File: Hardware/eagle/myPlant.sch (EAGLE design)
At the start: 38 parts, among them U1 SI7021, U2 ALS-PT19, U3 FSA3357, U4 TPS22860, U5 NCP1402, X1 ESP-12

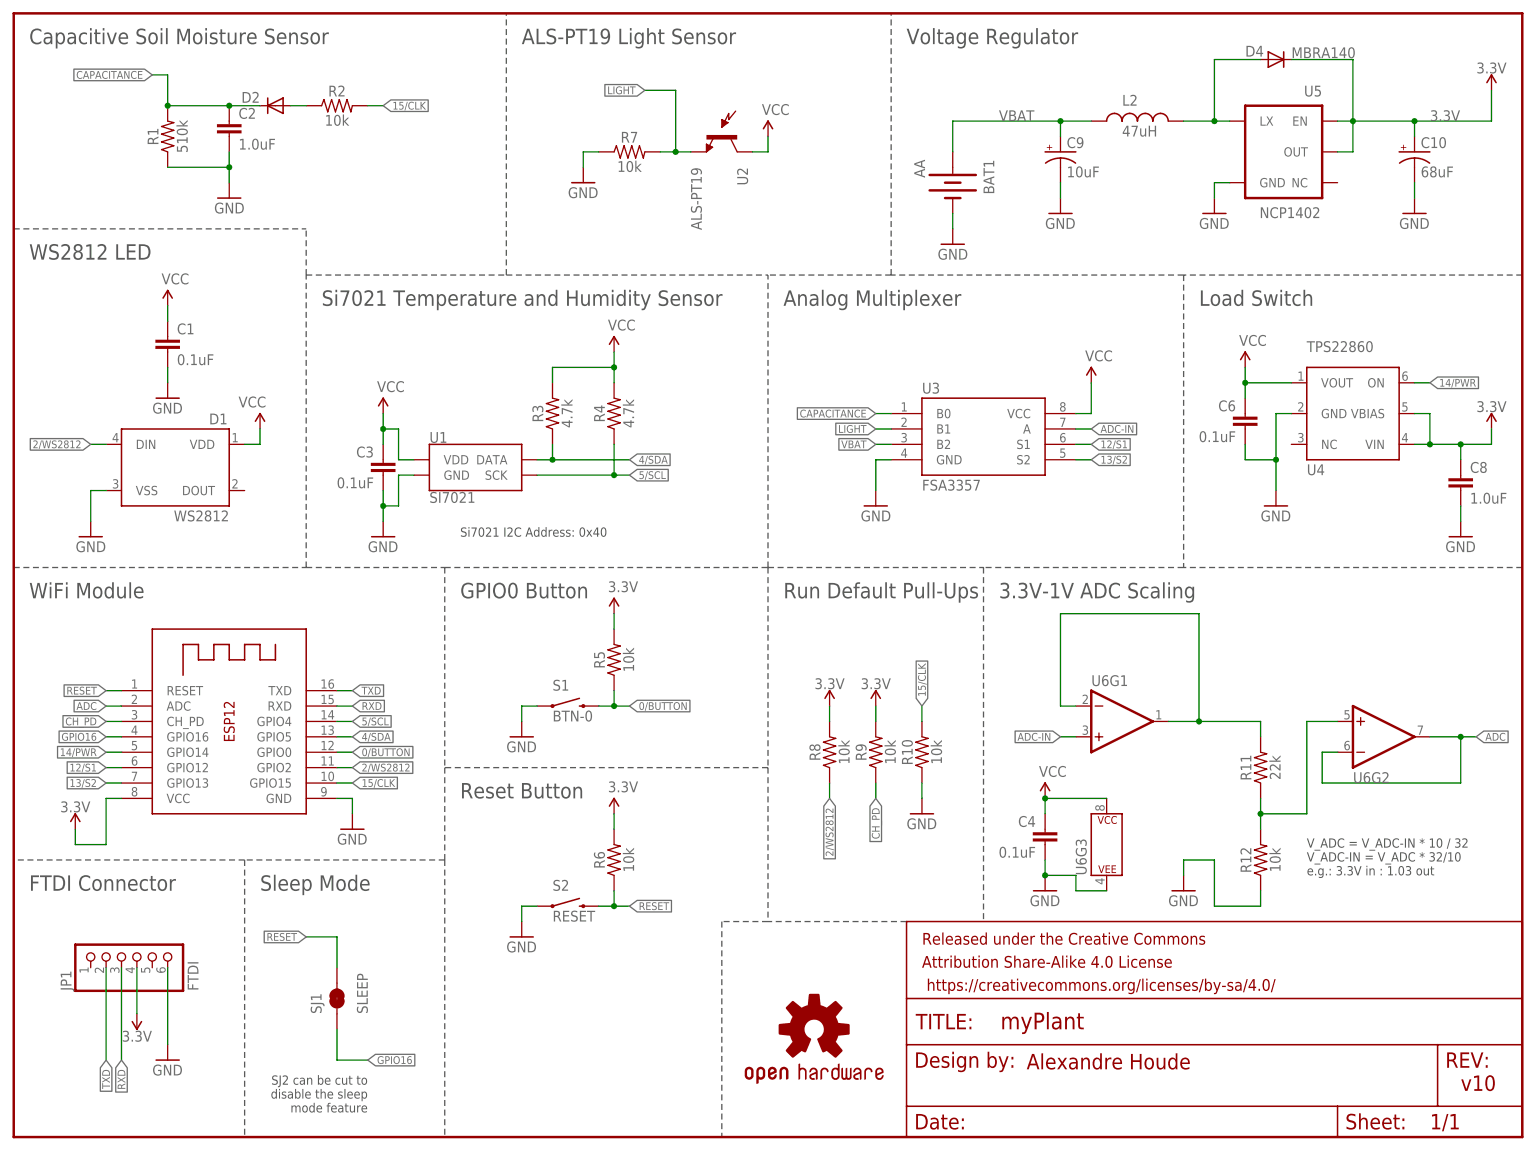
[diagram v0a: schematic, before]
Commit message: Corrected DRC errors
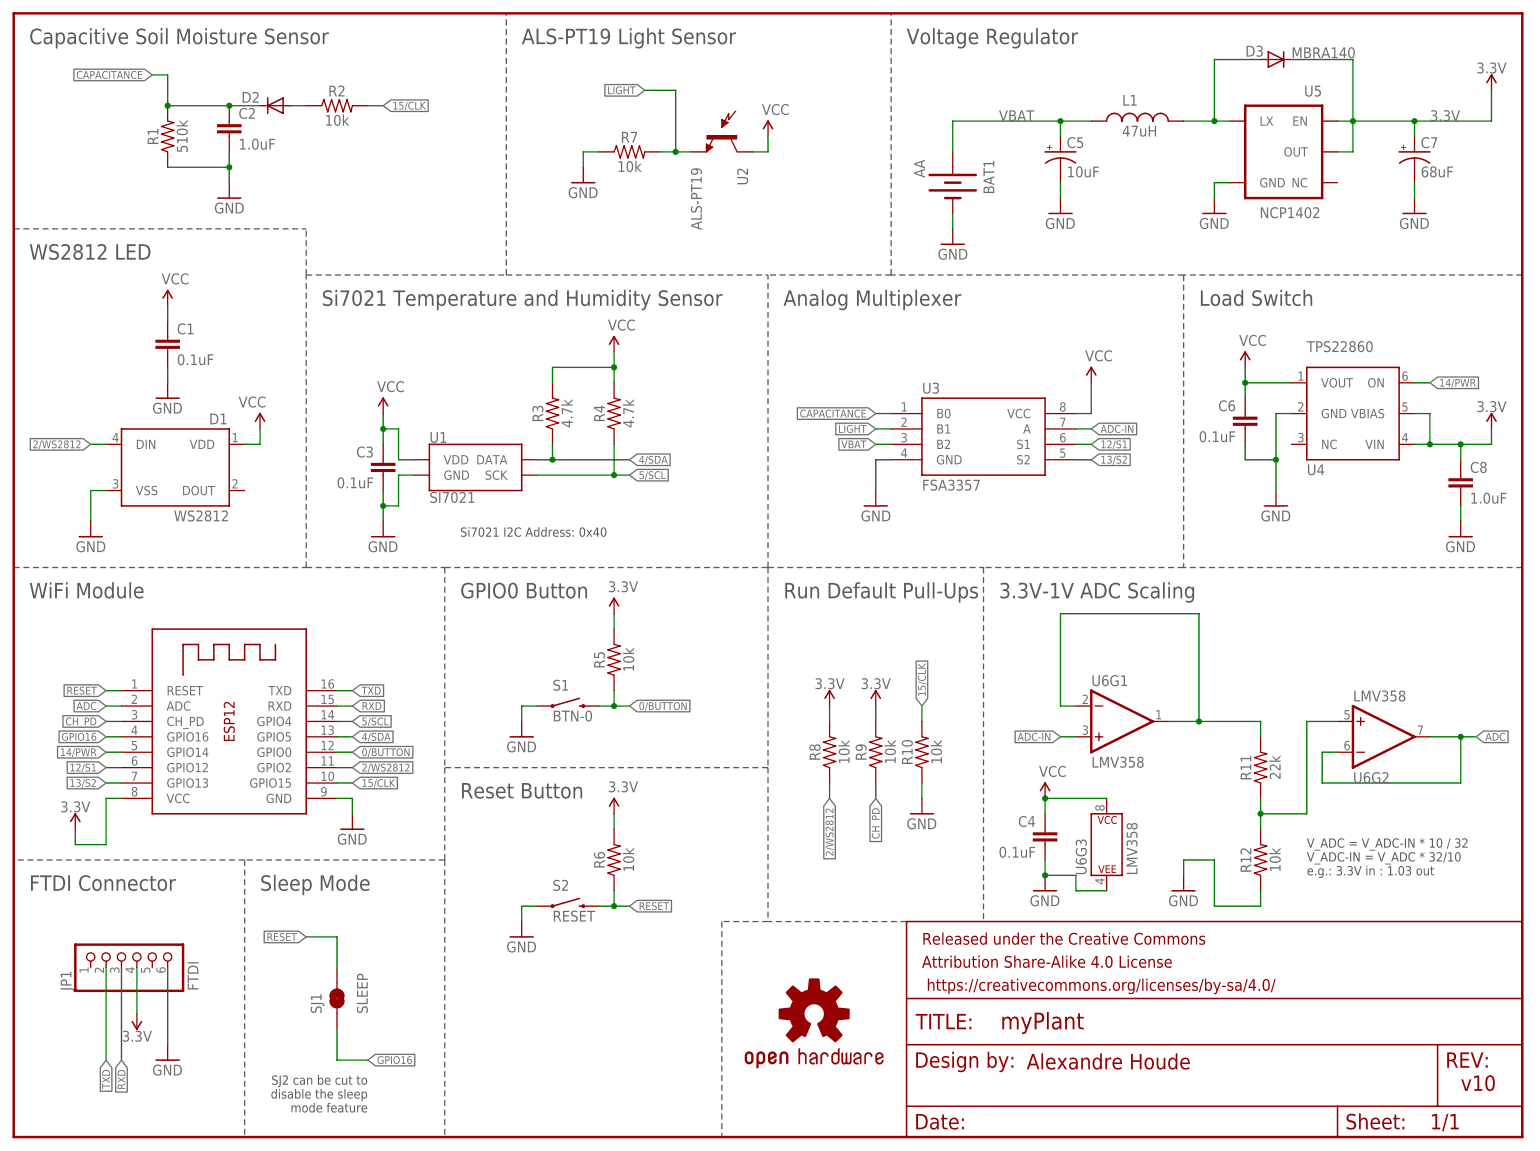
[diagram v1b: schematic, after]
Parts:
- removed LOGO1: OSHW-LOGOM, SparkFun-Aesthetics:OSHW-LOGOM
- added LOGO2: OSHW-LOGOS, SparkFun-Aesthetics:OSHW-LOGOS
- U6: value (none) -> LMV358
- renumbered C10 to C7, C9 to C5, D4 to D3, L2 to L1
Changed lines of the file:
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@@
 <?xml version="1.0" encoding="utf-8"?>
 <!DOCTYPE eagle SYSTEM "eagle.dtd">
-<eagle version="8.2.1">
+<eagle version="8.2.2">
 <drawing>
 <settings>
@@
 </layers>
 <schematic xreflabel="%F%N/%S.%C%R" xrefpart="/%S.%C%R">
-<description>Plant watering alarm v2.4</description>
 <attributes>
 </attributes>
@@
 <part name="GND20" library="SparkFun-Aesthetics" deviceset="GND" device=""/>
 <part name="FRAME1" library="SparkFun-Aesthetics" deviceset="FRAME-LETTER" device=""/>
-<part name="LOGO1" library="SparkFun-Aesthetics" deviceset="OSHW-LOGO" device="M"/>
 <part name="SUPPLY16" library="SparkFun-PowerSymbols" deviceset="3.3V" device=""/>
 <part name="SUPPLY17" library="SparkFun-PowerSymbols" deviceset="3.3V" device=""/>
@@
 <part name="C4" library="SparkFun-Capacitors" deviceset="0.1UF" device="-0603-25V-(+80/-20%)" value="0.1uF"/>
 <part name="U5" library="SparkFun" deviceset="V_REG_NCP1400" device="SOT23-5" value="NCP1402"/>
-<part name="D4" library="SparkFun" deviceset="DIODE" device="SMA" value="MBRA140"/>
-<part name="C9" library="SparkFun" deviceset="CAP_POL" device="1206" value="10uF"/>
-<part name="C10" library="SparkFun" deviceset="CAP_POL" device="3528" value="68uF"/>
-<part name="L2" library="SparkFun" deviceset="INDUCTOR" device="CR54" value="47uH"/>
+<part name="D3" library="SparkFun" deviceset="DIODE" device="SMA" value="MBRA140"/>
+<part name="C5" library="SparkFun" deviceset="CAP_POL" device="1206" value="10uF"/>
+<part name="C7" library="SparkFun" deviceset="CAP_POL" device="3528" value="68uF"/>
+<part name="L1" library="SparkFun" deviceset="INDUCTOR" device="CR54" value="47uH"/>
 <part name="GND22" library="SparkFun" deviceset="GND" device=""/>
 <part name="GND23" library="SparkFun" deviceset="GND" device=""/>
 <part name="GND24" library="SparkFun" deviceset="GND" device=""/>
-<part name="U6" library="SparkFun-IC-Amplifiers" deviceset="LMV358" device=""/>
+<part name="U6" library="SparkFun-IC-Amplifiers" deviceset="LMV358" device="" value="LMV358"/>
+<part name="LOGO2" library="SparkFun-Aesthetics" deviceset="OSHW-LOGO" device="S" value="OSHW-LOGOS"/>
 </parts>
 <sheets>
 <sheet>
-<description>Plant watering alarm v1.0</description>
 <plain>
 <text x="73.66" y="99.06" size="1.524" layer="97">Si7021 I2C Address: 0x40</text>
@@
 <instance part="FRAME1" gate="G$1" x="0" y="0"/>
 <instance part="FRAME1" gate="V" x="147.32" y="0"/>
-<instance part="LOGO1" gate="G$1" x="132.08" y="17.78"/>
 <instance part="SUPPLY16" gate="G$1" x="243.84" y="172.72"/>
 <instance part="SUPPLY17" gate="G$1" x="243.84" y="116.84"/>
@@
 <instance part="C4" gate="G$1" x="170.18" y="48.26" rot="MR0"/>
 <instance part="U5" gate="G$1" x="210.82" y="162.56" rot="MR0"/>
-<instance part="D4" gate="G$1" x="208.28" y="177.8" smashed="yes">
+<instance part="D3" gate="G$1" x="208.28" y="177.8" smashed="yes">
 <attribute name="NAME" x="203.2" y="178.2826" size="1.778" layer="95"/>
 <attribute name="VALUE" x="210.82" y="178.0286" size="1.778" layer="96"/>
 </instance>
-<instance part="C9" gate="G$1" x="172.72" y="162.56"/>
-<instance part="C10" gate="G$1" x="231.14" y="162.56"/>
-<instance part="L2" gate="G$1" x="185.42" y="167.64" smashed="yes" rot="R90">
+<instance part="C5" gate="G$1" x="172.72" y="162.56"/>
+<instance part="C7" gate="G$1" x="231.14" y="162.56"/>
+<instance part="L1" gate="G$1" x="185.42" y="167.64" smashed="yes" rot="R90">
 <attribute name="NAME" x="182.88" y="170.18" size="1.778" layer="95"/>
 <attribute name="VALUE" x="182.88" y="165.1" size="1.778" layer="96"/>
@@
 <instance part="U6" gate="G2" x="226.06" y="66.04" rot="MR180"/>
 <instance part="U6" gate="G3" x="180.34" y="48.26"/>
+<instance part="LOGO2" gate="G$1" x="132.08" y="20.32"/>
 </instances>
 <busses>
@@
 <segment>
 <wire x1="231.14" y1="157.48" x2="231.14" y2="154.94" width="0.1524" layer="91"/>
-<pinref part="C10" gate="G$1" pin="-"/>
+<pinref part="C7" gate="G$1" pin="-"/>
 <pinref part="GND24" gate="1" pin="GND"/>
 </segment>
@@
 <segment>
 <wire x1="172.72" y1="157.48" x2="172.72" y2="154.94" width="0.1524" layer="91"/>
-<pinref part="C9" gate="G$1" pin="-"/>
+<pinref part="C5" gate="G$1" pin="-"/>
 <pinref part="GND22" gate="1" pin="GND"/>
 </segment>
@@
 <pinref part="U5" gate="G$1" pin="EN"/>
 <pinref part="U5" gate="G$1" pin="OUT"/>
-<pinref part="D4" gate="G$1" pin="C"/>
-<pinref part="C10" gate="G$1" pin="+"/>
+<pinref part="D3" gate="G$1" pin="C"/>
+<pinref part="C7" gate="G$1" pin="+"/>
 </segment>
 </net>
@@
 <junction x="198.12" y="167.64"/>
 <pinref part="U5" gate="G$1" pin="LX"/>
-<pinref part="D4" gate="G$1" pin="A"/>
-<pinref part="L2" gate="G$1" pin="2"/>
+<pinref part="D3" gate="G$1" pin="A"/>
+<pinref part="L1" gate="G$1" pin="2"/>
 </segment>
 </net>
@@
 <junction x="172.72" y="167.64"/>
 <label x="162.56" y="167.64" size="1.778" layer="95"/>
-<pinref part="L2" gate="G$1" pin="1"/>
-<pinref part="C9" gate="G$1" pin="+"/>
+<pinref part="L1" gate="G$1" pin="1"/>
+<pinref part="C5" gate="G$1" pin="+"/>
 <pinref part="BAT1" gate="G$1" pin="+"/>
 <wire x1="154.94" y1="162.56" x2="154.94" y2="167.64" width="0.1524" layer="91"/>
